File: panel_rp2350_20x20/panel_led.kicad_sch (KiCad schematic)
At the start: 420 parts

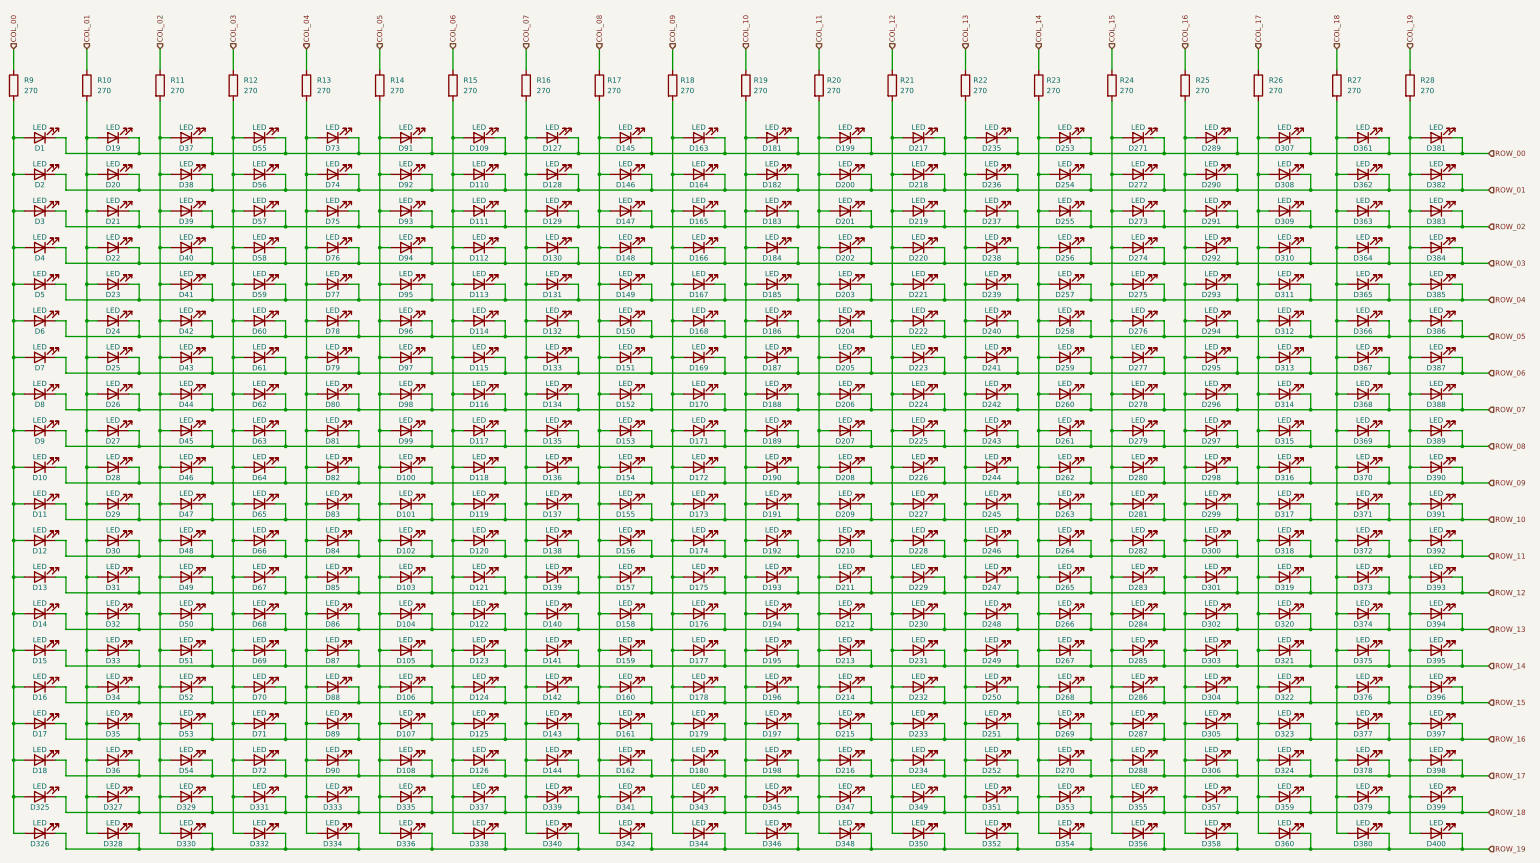
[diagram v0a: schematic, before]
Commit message: More work on rp2350 20x20 panel.
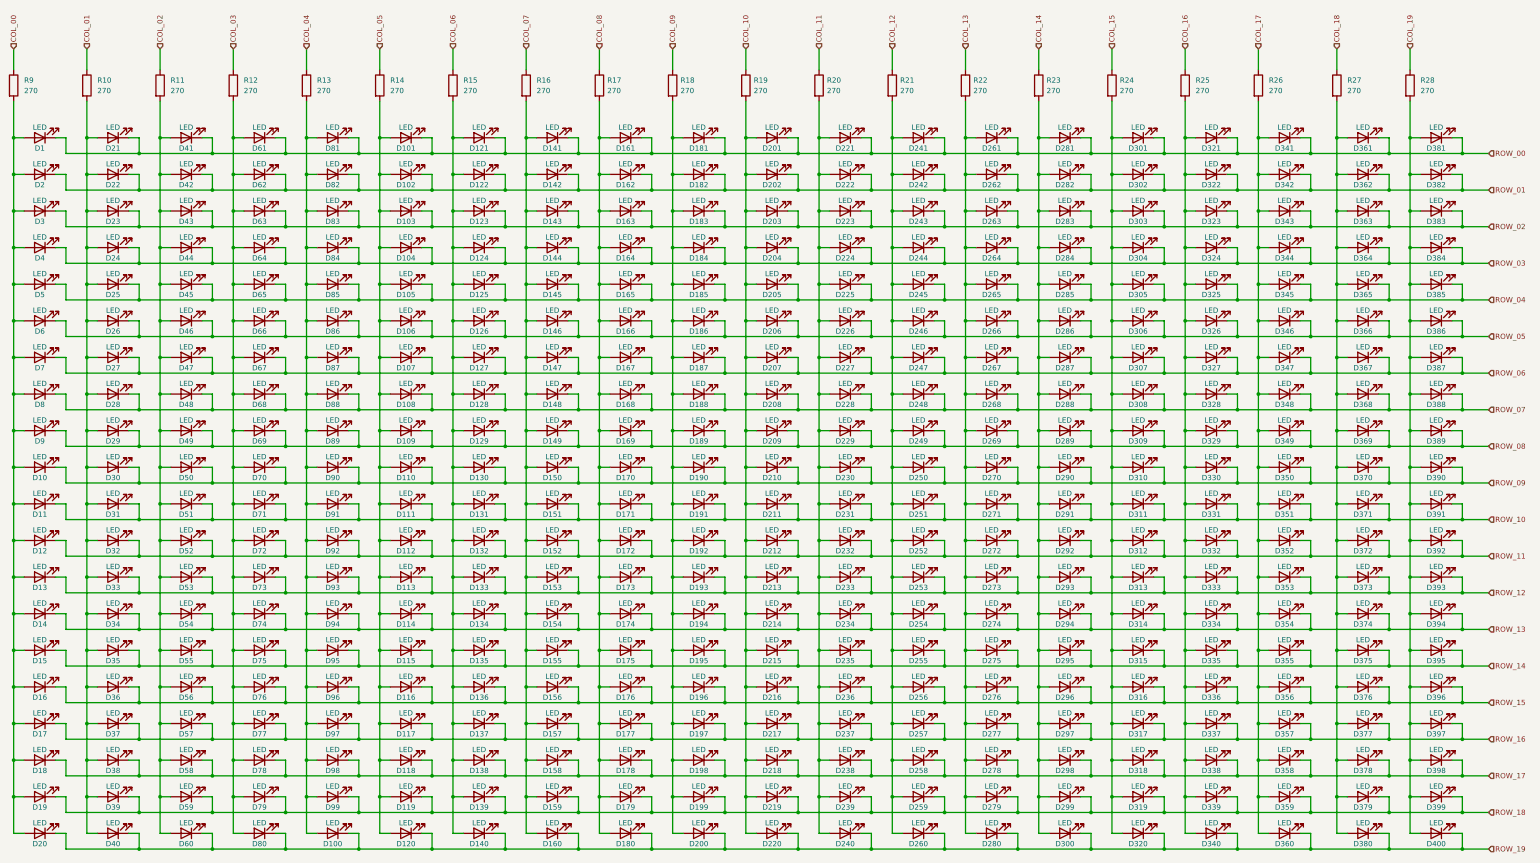
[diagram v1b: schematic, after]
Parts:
- renumbered D334 to D100, D91 to D101, D92 to D102, D93 to D103, D94 to D104, D95 to D105, D96 to D106, D97 to D107, D98 to D108, D99 to D109, D100 to D110, D101 to D111, D102 to D112, D103 to D113, D104 to D114, D105 to D115, D106 to D116, D107 to D117, D108 to D118, D335 to D119, D336 to D120, D109 to D121, D110 to D122, D111 to D123, D112 to D124, D113 to D125, D114 to D126, D115 to D127, D116 to D128, D117 to D129, D118 to D130, D119 to D131, D120 to D132, D121 to D133, D122 to D134, D123 to D135, D124 to D136, D125 to D137, D126 to D138, D337 to D139, D338 to D140, D127 to D141, D128 to D142, D129 to D143, D130 to D144, D131 to D145, D132 to D146, D133 to D147, D134 to D148, D135 to D149, D136 to D150, D137 to D151, D138 to D152, D139 to D153, D140 to D154, D141 to D155, D142 to D156, D143 to D157, D144 to D158, D339 to D159, D340 to D160, D145 to D161, D146 to D162, D147 to D163, D148 to D164, D149 to D165, D150 to D166, D151 to D167, D152 to D168, D153 to D169, D154 to D170, D155 to D171, D156 to D172, D157 to D173, D158 to D174, D159 to D175, D160 to D176, D161 to D177, D162 to D178, D341 to D179, D342 to D180, D163 to D181, D164 to D182, D165 to D183, D166 to D184, D167 to D185, D168 to D186, D169 to D187, D170 to D188, D171 to D189, D325 to D19, D172 to D190, D173 to D191, D174 to D192, D175 to D193, D176 to D194, D177 to D195, D178 to D196, D179 to D197, D180 to D198, D343 to D199, D326 to D20, D344 to D200, D181 to D201, D182 to D202, D183 to D203, D184 to D204, D185 to D205, D186 to D206, D187 to D207, D188 to D208, D189 to D209, D19 to D21, D190 to D210, D191 to D211, D192 to D212, D193 to D213, D194 to D214, D195 to D215, D196 to D216, D197 to D217, D198 to D218, D345 to D219, D20 to D22, D346 to D220, D199 to D221, D200 to D222, D201 to D223, D202 to D224, D203 to D225, D204 to D226, D205 to D227, D206 to D228, D207 to D229, D21 to D23, D208 to D230, D209 to D231, D210 to D232, D211 to D233, D212 to D234, D213 to D235, D214 to D236, D215 to D237, D216 to D238, D347 to D239, D22 to D24, D348 to D240, D217 to D241, D218 to D242, D219 to D243, D220 to D244, D221 to D245, D222 to D246, D223 to D247, D224 to D248, D225 to D249, D23 to D25, D226 to D250, D227 to D251, D228 to D252, D229 to D253, D230 to D254, D231 to D255, D232 to D256, D233 to D257, D234 to D258, D349 to D259, D24 to D26, D350 to D260, D235 to D261, D236 to D262, D237 to D263, D238 to D264, D239 to D265, D240 to D266, D241 to D267, D242 to D268, D243 to D269, D25 to D27, D244 to D270, D245 to D271, D246 to D272, D247 to D273, D248 to D274, D249 to D275, D250 to D276, D251 to D277, D252 to D278, D351 to D279, D26 to D28, D352 to D280, D253 to D281, D254 to D282, D255 to D283, D256 to D284, D257 to D285, D258 to D286, D259 to D287, D260 to D288, D261 to D289, D27 to D29, D262 to D290, D263 to D291, D264 to D292, D265 to D293, D266 to D294, D267 to D295, D268 to D296, D269 to D297, D270 to D298, D353 to D299, D28 to D30, D354 to D300, D271 to D301, D272 to D302, D273 to D303, D274 to D304, D275 to D305, D276 to D306, D277 to D307, D278 to D308, D279 to D309, D29 to D31, D280 to D310, D281 to D311, D282 to D312, D283 to D313, D284 to D314, D285 to D315, D286 to D316, D287 to D317, D288 to D318, D355 to D319, D30 to D32, D356 to D320, D289 to D321, D290 to D322, D291 to D323, D292 to D324, D293 to D325, D294 to D326, D295 to D327, D296 to D328, D297 to D329, D31 to D33, D298 to D330, D299 to D331, D300 to D332, D301 to D333, D302 to D334, D303 to D335, D304 to D336, D305 to D337, D306 to D338, D357 to D339, D32 to D34, D358 to D340, D307 to D341, D308 to D342, D309 to D343, D310 to D344, D311 to D345, D312 to D346, D313 to D347, D314 to D348, D315 to D349, D33 to D35, D316 to D350, D317 to D351, D318 to D352, D319 to D353, D320 to D354, D321 to D355, D322 to D356, D323 to D357, D324 to D358, D34 to D36, D35 to D37, D36 to D38, D327 to D39, D328 to D40, D37 to D41, D38 to D42, D39 to D43, D40 to D44, D41 to D45, D42 to D46, D43 to D47, D44 to D48, D45 to D49, D46 to D50, D47 to D51, D48 to D52, D49 to D53, D50 to D54, D51 to D55, D52 to D56, D53 to D57, D54 to D58, D329 to D59, D330 to D60, D55 to D61, D56 to D62, D57 to D63, D58 to D64, D59 to D65, D60 to D66, D61 to D67, D62 to D68, D63 to D69, D64 to D70, D65 to D71, D66 to D72, D67 to D73, D68 to D74, D69 to D75, D70 to D76, D71 to D77, D72 to D78, D331 to D79, D332 to D80, D73 to D81, D74 to D82, D75 to D83, D76 to D84, D77 to D85, D78 to D86, D79 to D87, D80 to D88, D81 to D89, D82 to D90, D83 to D91, D84 to D92, D85 to D93, D86 to D94, D87 to D95, D88 to D96, D89 to D97, D90 to D98, D333 to D99

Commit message: Worked on layout and routing for  rp2350 20x20 array panel.
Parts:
- D1, D10, D100, D11, D12, D13, D14, D15, D16, D161, D162, D163, D164, D165, D166, D167, D168, D169, D17, D170, D171, D172, D173, D174, D175, D176, D177, D178, D179, D18, D180, D19, D2, D20, D241, D242, D243, D244, D245, D246, D247, D248, D249, D250, D251, D252, D253, D254, D255, D256, D257, D258, D259, D260, D3, D321, D322, D323, D324, D325, D326, D327, D328, D329, D330, D331, D332, D333, D334, D335, D336, D337, D338, D339, D340, D4, D5, D6, D7, D8, D81, D82, D83, D84, D85, D86, D87, D88, D89, D9, D90, D91, D92, D93, D94, D95, D96, D97, D98, D99: value LED -> LED_T0; symbol Device:LED -> panel_custom:LED_TYPE_0
- D101, D102, D103, D104, D105, D106, D107, D108, D109, D110, D111, D112, D113, D114, D115, D116, D117, D118, D119, D120, D181, D182, D183, D184, D185, D186, D187, D188, D189, D190, D191, D192, D193, D194, D195, D196, D197, D198, D199, D200, D21, D22, D23, D24, D25, D26, D261, D262, D263, D264, D265, D266, D267, D268, D269, D27, D270, D271, D272, D273, D274, D275, D276, D277, D278, D279, D28, D280, D29, D30, D31, D32, D33, D34, D341, D342, D343, D344, D345, D346, D347, D348, D349, D35, D350, D351, D352, D353, D354, D355, D356, D357, D358, D359, D36, D360, D37, D38, D39, D40: value LED -> LED_T1; symbol Device:LED -> panel_custom:LED_TYPE_1
- D121, D122, D123, D124, D125, D126, D127, D128, D129, D130, D131, D132, D133, D134, D135, D136, D137, D138, D139, D140, D201, D202, D203, D204, D205, D206, D207, D208, D209, D210, D211, D212, D213, D214, D215, D216, D217, D218, D219, D220, D281, D282, D283, D284, D285, D286, D287, D288, D289, D290, D291, D292, D293, D294, D295, D296, D297, D298, D299, D300, D361, D362, D363, D364, D365, D366, D367, D368, D369, D370, D371, D372, D373, D374, D375, D376, D377, D378, D379, D380, D41, D42, D43, D44, D45, D46, D47, D48, D49, D50, D51, D52, D53, D54, D55, D56, D57, D58, D59, D60: value LED -> LED_T2; symbol Device:LED -> panel_custom:LED_TYPE_2
- D141, D142, D143, D144, D145, D146, D147, D148, D149, D150, D151, D152, D153, D154, D155, D156, D157, D158, D159, D160, D221, D222, D223, D224, D225, D226, D227, D228, D229, D230, D231, D232, D233, D234, D235, D236, D237, D238, D239, D240, D301, D302, D303, D304, D305, D306, D307, D308, D309, D310, D311, D312, D313, D314, D315, D316, D317, D318, D319, D320, D381, D382, D383, D384, D385, D386, D387, D388, D389, D390, D391, D392, D393, D394, D395, D396, D397, D398, D399, D400, D61, D62, D63, D64, D65, D66, D67, D68, D69, D70, D71, D72, D73, D74, D75, D76, D77, D78, D79, D80: value LED -> LED_T3; symbol Device:LED -> panel_custom:LED_TYPE_3

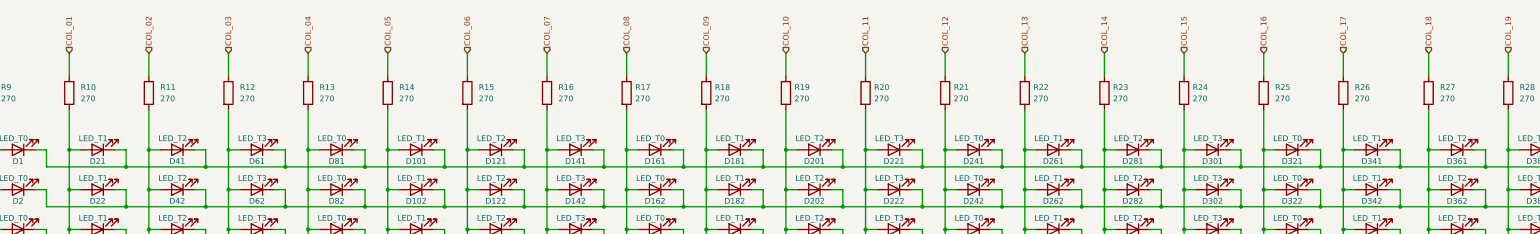
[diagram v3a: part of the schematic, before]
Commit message: Worked on routing, layout and fab setup for rp2354b 20x20 panel.
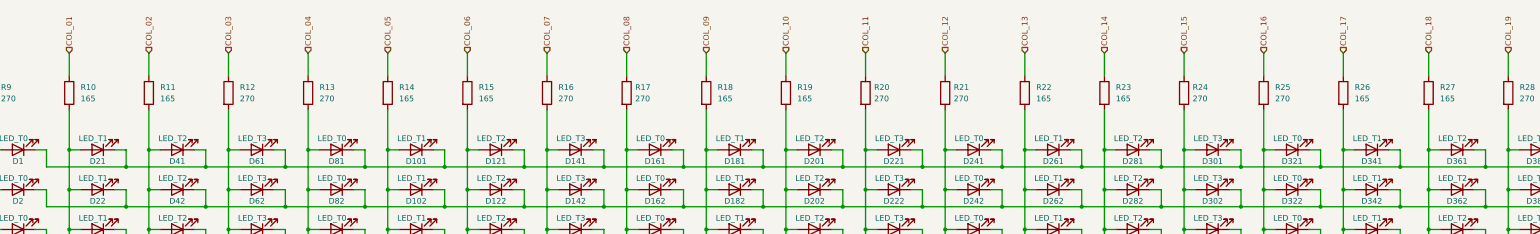
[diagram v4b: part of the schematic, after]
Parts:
- D1, D10, D100, D11, D12, D13, D14, D141, D142, D143, D144, D145, D146, D147, D148, D149, D15, D150, D151, D152, D153, D154, D155, D156, D157, D158, D159, D16, D160, D161, D162, D163, D164, D165, D166, D167, D168, D169, D17, D170, D171, D172, D173, D174, D175, D176, D177, D178, D179, D18, D180, D19, D2, D20, D221, D222, D223, D224, D225, D226, D227, D228, D229, D230, D231, D232, D233, D234, D235, D236, D237, D238, D239, D240, D241, D242, D243, D244, D245, D246, D247, D248, D249, D250, D251, D252, D253, D254, D255, D256, D257, D258, D259, D260, D3, D301, D302, D303, D304, D305, D306, D307, D308, D309, D310, D311, D312, D313, D314, D315, D316, D317, D318, D319, D320, D321, D322, D323, D324, D325, D326, D327, D328, D329, D330, D331, D332, D333, D334, D335, D336, D337, D338, D339, D340, D381, D382, D383, D384, D385, D386, D387, D388, D389, D390, D391, D392, D393, D394, D395, D396, D397, D398, D399, D4, D400, D5, D6, D61, D62, D63, D64, D65, D66, D67, D68, D69, D7, D70, D71, D72, D73, D74, D75, D76, D77, D78, D79, D8, D80, D81, D82, D83, D84, D85, D86, D87, D88, D89, D9, D90, D91, D92, D93, D94, D95, D96, D97, D98, D99: LCSC Part # (none) -> C273601
- D101, D102, D103, D104, D105, D106, D107, D108, D109, D110, D111, D112, D113, D114, D115, D116, D117, D118, D119, D120, D121, D122, D123, D124, D125, D126, D127, D128, D129, D130, D131, D132, D133, D134, D135, D136, D137, D138, D139, D140, D181, D182, D183, D184, D185, D186, D187, D188, D189, D190, D191, D192, D193, D194, D195, D196, D197, D198, D199, D200, D201, D202, D203, D204, D205, D206, D207, D208, D209, D21, D210, D211, D212, D213, D214, D215, D216, D217, D218, D219, D22, D220, D23, D24, D25, D26, D261, D262, D263, D264, D265, D266, D267, D268, D269, D27, D270, D271, D272, D273, D274, D275, D276, D277, D278, D279, D28, D280, D281, D282, D283, D284, D285, D286, D287, D288, D289, D29, D290, D291, D292, D293, D294, D295, D296, D297, D298, D299, D30, D300, D31, D32, D33, D34, D341, D342, D343, D344, D345, D346, D347, D348, D349, D35, D350, D351, D352, D353, D354, D355, D356, D357, D358, D359, D36, D360, D361, D362, D363, D364, D365, D366, D367, D368, D369, D37, D370, D371, D372, D373, D374, D375, D376, D377, D378, D379, D38, D380, D39, D40, D41, D42, D43, D44, D45, D46, D47, D48, D49, D50, D51, D52, D53, D54, D55, D56, D57, D58, D59, D60: LCSC Part # (none) -> C131223
- R10, R11, R14, R15, R18, R19, R22, R23, R26, R27: value 270 -> 165; LCSC Part # (none) -> C320715
- R12, R13, R16, R17, R20, R21, R24, R25, R28, R9: LCSC Part # (none) -> C320799
